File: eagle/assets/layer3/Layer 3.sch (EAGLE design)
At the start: 84 parts, among them Q2 AO3402, X1 SM06B-SRSS-TB, Y1 8MHz

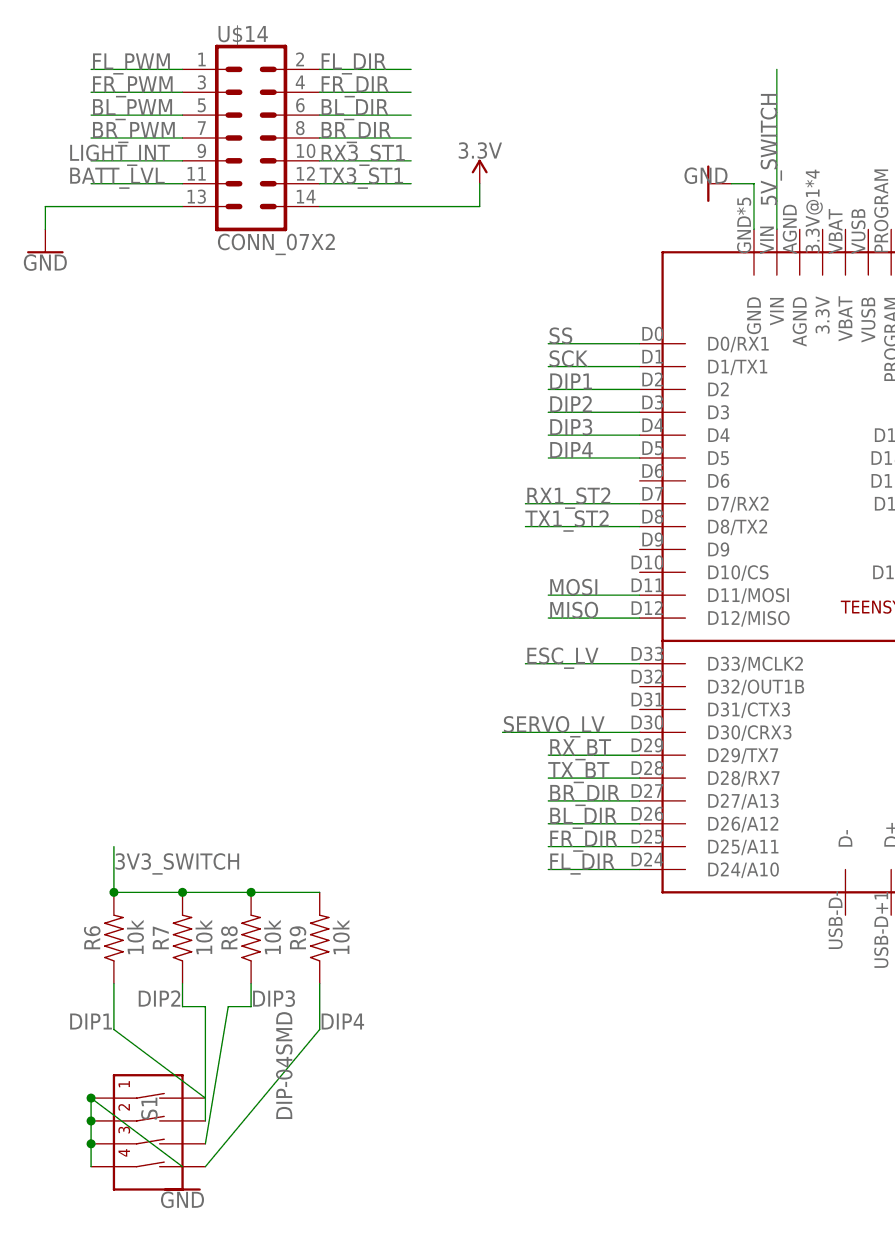
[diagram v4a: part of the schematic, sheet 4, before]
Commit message: added teensy 4 lbr
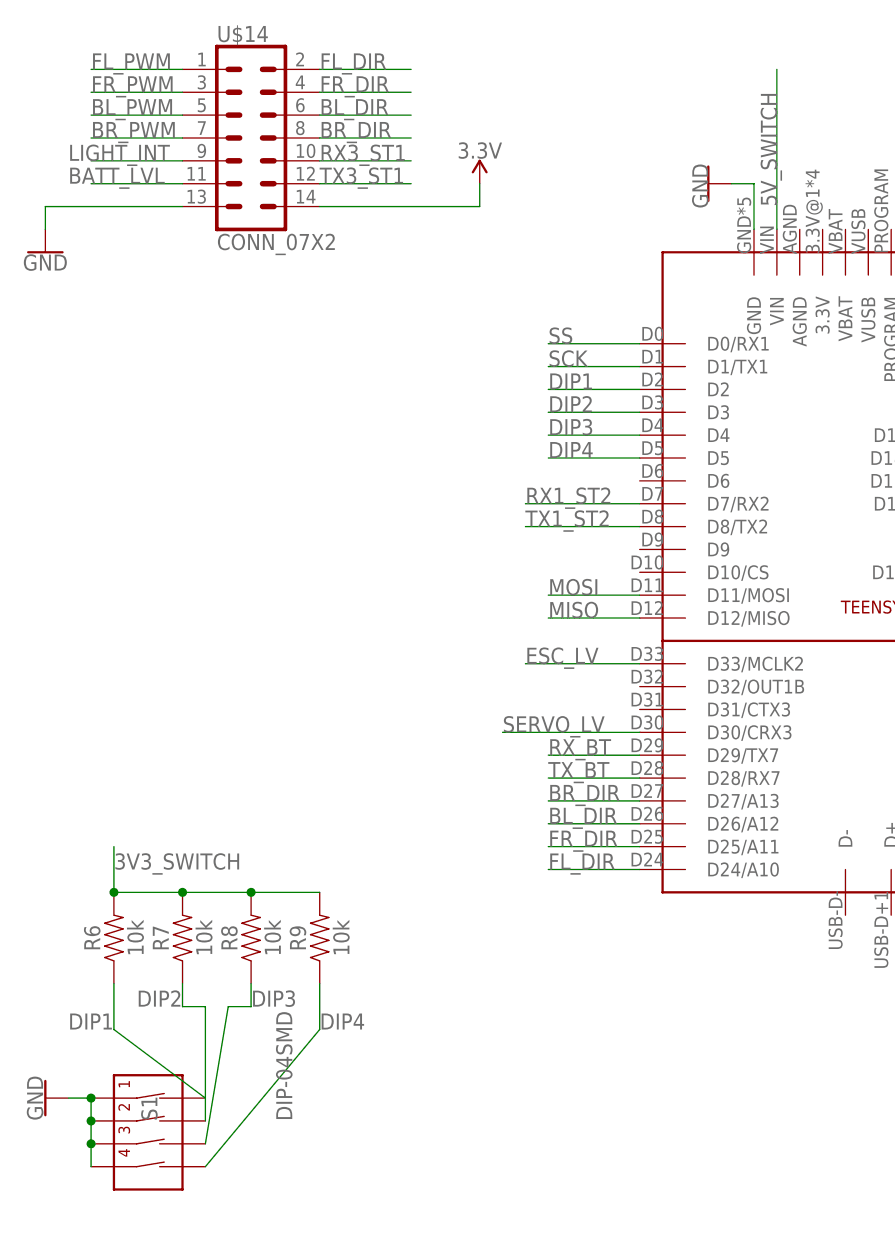
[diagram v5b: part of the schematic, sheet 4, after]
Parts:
- renumbered U$1 to TEENSY4
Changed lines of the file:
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@@
 <part name="R11" library="SparkFun-Resistors" library_urn="urn:adsk.eagle:library:532" deviceset="4.7KOHM" device="-0603-1/10W-1%" package3d_urn="urn:adsk.eagle:package:39650/1" value="4.7k"/>
 <part name="GND34" library="SparkFun-PowerSymbols" library_urn="urn:adsk.eagle:library:530" deviceset="GND" device=""/>
-<part name="U$1" library="Teensy-4.0" deviceset="TEENSY-4.0-FULL-BREAKOUT-PINS" device=""/>
+<part name="TEENSY4" library="Teensy-4.0" deviceset="TEENSY-4.0-FULL-BREAKOUT-PINS" device=""/>
 <part name="GND35" library="SparkFun-PowerSymbols" library_urn="urn:adsk.eagle:library:530" deviceset="GND" device=""/>
 </parts>
@@
 <attribute name="VALUE" x="43.434" y="38.1" size="1.778" layer="96" font="vector" rot="R90" align="top-left"/>
 </instance>
-<instance part="GND38" gate="1" x="33.02" y="30.48" smashed="yes">
-<attribute name="VALUE" x="33.02" y="30.226" size="1.778" layer="96" align="top-center"/>
+<instance part="GND38" gate="1" x="17.78" y="40.64" smashed="yes" rot="R270">
+<attribute name="VALUE" x="17.526" y="40.64" size="1.778" layer="96" rot="R270" align="top-center"/>
 </instance>
 <instance part="R6" gate="G$1" x="25.4" y="58.42" smashed="yes" rot="R90">
@@
 <attribute name="VALUE" x="246.38" y="106.934" size="1.778" layer="96" align="bottom-center"/>
 </instance>
-<instance part="U$1" gate="G$1" x="86.36" y="63.5" smashed="yes"/>
+<instance part="TEENSY4" gate="G$1" x="86.36" y="63.5" smashed="yes"/>
 <instance part="GND35" gate="1" x="91.44" y="142.24" smashed="yes" rot="R270">
-<attribute name="VALUE" x="91.186" y="142.24" size="1.778" layer="96" rot="R180" align="top-center"/>
+<attribute name="VALUE" x="91.44" y="141.986" size="1.778" layer="96" rot="R270" align="top-center"/>
 </instance>
 </instances>
@@
 </segment>
 <segment>
-<pinref part="U$1" gate="G$1" pin="D24/A10"/>
+<pinref part="TEENSY4" gate="G$1" pin="D24/A10"/>
 <wire x1="83.82" y1="66.04" x2="73.66" y2="66.04" width="0.1524" layer="91"/>
 <label x="73.66" y="66.04" size="1.778" layer="95"/>
@@
 </segment>
 <segment>
-<pinref part="U$1" gate="G$1" pin="D25/A11"/>
+<pinref part="TEENSY4" gate="G$1" pin="D25/A11"/>
 <wire x1="83.82" y1="68.58" x2="73.66" y2="68.58" width="0.1524" layer="91"/>
 <label x="73.66" y="68.58" size="1.778" layer="95"/>
@@
 </segment>
 <segment>
-<pinref part="U$1" gate="G$1" pin="D26/A12"/>
+<pinref part="TEENSY4" gate="G$1" pin="D26/A12"/>
 <wire x1="83.82" y1="71.12" x2="73.66" y2="71.12" width="0.1524" layer="91"/>
 <label x="73.66" y="71.12" size="1.778" layer="95"/>
@@
 </segment>
 <segment>
-<pinref part="U$1" gate="G$1" pin="D27/A13"/>
+<pinref part="TEENSY4" gate="G$1" pin="D27/A13"/>
 <wire x1="83.82" y1="73.66" x2="73.66" y2="73.66" width="0.1524" layer="91"/>
 <label x="73.66" y="73.66" size="1.778" layer="95"/>
@@
 <wire x1="129.54" y1="101.6" x2="147.32" y2="101.6" width="0.1524" layer="91"/>
 <label x="147.32" y="103.378" size="1.778" layer="95" rot="R180"/>
-<pinref part="U$1" gate="G$1" pin="D14/A0"/>
+<pinref part="TEENSY4" gate="G$1" pin="D14/A0"/>
 </segment>
 </net>
@@
 <wire x1="129.54" y1="99.06" x2="147.32" y2="99.06" width="0.1524" layer="91"/>
 <label x="147.32" y="100.838" size="1.778" layer="95" rot="R180"/>
-<pinref part="U$1" gate="G$1" pin="D13/SCK/LED"/>
+<pinref part="TEENSY4" gate="G$1" pin="D13/SCK/LED"/>
 </segment>
 </net>
@@
 </segment>
 <segment>
-<pinref part="U$1" gate="G$1" pin="D18/A4/SDA0"/>
+<pinref part="TEENSY4" gate="G$1" pin="D18/A4/SDA0"/>
 <wire x1="129.54" y1="111.76" x2="147.32" y2="111.76" width="0.1524" layer="91"/>
 <label x="134.62" y="111.76" size="1.778" layer="95"/>
@@
 </segment>
 <segment>
-<pinref part="U$1" gate="G$1" pin="D19/A5/SCL0"/>
+<pinref part="TEENSY4" gate="G$1" pin="D19/A5/SCL0"/>
 <wire x1="129.54" y1="114.3" x2="147.32" y2="114.3" width="0.1524" layer="91"/>
 <label x="134.62" y="114.3" size="1.778" layer="95"/>
@@
 </segment>
 <segment>
-<pinref part="U$1" gate="G$1" pin="D20/A6"/>
+<pinref part="TEENSY4" gate="G$1" pin="D20/A6"/>
 <wire x1="129.54" y1="116.84" x2="147.32" y2="116.84" width="0.1524" layer="91"/>
 <label x="134.62" y="116.84" size="1.778" layer="95"/>
@@
 </segment>
 <segment>
-<pinref part="U$1" gate="G$1" pin="D21/A7"/>
+<pinref part="TEENSY4" gate="G$1" pin="D21/A7"/>
 <wire x1="129.54" y1="119.38" x2="147.32" y2="119.38" width="0.1524" layer="91"/>
 <label x="134.62" y="119.38" size="1.778" layer="95"/>
@@
 <wire x1="129.54" y1="121.92" x2="147.32" y2="121.92" width="0.1524" layer="91"/>
 <label x="134.62" y="121.92" size="1.778" layer="95"/>
-<pinref part="U$1" gate="G$1" pin="D22/A8"/>
+<pinref part="TEENSY4" gate="G$1" pin="D22/A8"/>
 </segment>
 </net>
@@
 <wire x1="129.54" y1="124.46" x2="147.32" y2="124.46" width="0.1524" layer="91"/>
 <label x="134.62" y="124.46" size="1.778" layer="95"/>
-<pinref part="U$1" gate="G$1" pin="D23/A9"/>
+<pinref part="TEENSY4" gate="G$1" pin="D23/A9"/>
 </segment>
 </net>
@@
 <junction x="22.86" y="35.56"/>
 <pinref part="GND38" gate="1" pin="GND"/>
-<wire x1="22.86" y1="40.64" x2="33.02" y2="33.02" width="0.1524" layer="91"/>
+<wire x1="22.86" y1="40.64" x2="20.32" y2="40.64" width="0.1524" layer="91"/>
 <junction x="22.86" y="40.64"/>
 </segment>
@@
 </segment>
 <segment>
-<pinref part="U$1" gate="G$1" pin="GND"/>
+<pinref part="TEENSY4" gate="G$1" pin="GND"/>
 <wire x1="96.52" y1="137.16" x2="96.52" y2="142.24" width="0.1524" layer="91"/>
 <wire x1="96.52" y1="142.24" x2="93.98" y2="142.24" width="0.1524" layer="91"/>
@@
 </segment>
 <segment>
-<pinref part="U$1" gate="G$1" pin="VIN"/>
+<pinref part="TEENSY4" gate="G$1" pin="VIN"/>
 <wire x1="99.06" y1="137.16" x2="99.06" y2="154.94" width="0.1524" layer="91"/>
 <label x="99.06" y="139.7" size="1.778" layer="95" rot="R90"/>
@@
 </segment>
 <segment>
-<pinref part="U$1" gate="G$1" pin="D11/MOSI"/>
+<pinref part="TEENSY4" gate="G$1" pin="D11/MOSI"/>
 <wire x1="83.82" y1="96.52" x2="73.66" y2="96.52" width="0.1524" layer="91"/>
 <label x="73.66" y="96.52" size="1.778" layer="95"/>
@@
 </segment>
 <segment>
-<pinref part="U$1" gate="G$1" pin="D12/MISO"/>
+<pinref part="TEENSY4" gate="G$1" pin="D12/MISO"/>
 <wire x1="83.82" y1="93.98" x2="73.66" y2="93.98" width="0.1524" layer="91"/>
 <label x="73.66" y="93.98" size="1.778" layer="95"/>
@@
 </segment>
 <segment>
-<pinref part="U$1" gate="G$1" pin="D1/TX1"/>
+<pinref part="TEENSY4" gate="G$1" pin="D1/TX1"/>
 <wire x1="83.82" y1="121.92" x2="73.66" y2="121.92" width="0.1524" layer="91"/>
 <label x="73.66" y="121.92" size="1.778" layer="95"/>
@@
 </segment>
 <segment>
-<pinref part="U$1" gate="G$1" pin="D0/RX1"/>
+<pinref part="TEENSY4" gate="G$1" pin="D0/RX1"/>
 <wire x1="83.82" y1="124.46" x2="73.66" y2="124.46" width="0.1524" layer="91"/>
 <label x="73.66" y="124.46" size="1.778" layer="95"/>
@@
 <wire x1="129.54" y1="106.68" x2="147.32" y2="106.68" width="0.1524" layer="91"/>
 <label x="134.62" y="106.68" size="1.778" layer="95"/>
-<pinref part="U$1" gate="G$1" pin="D16/A2/SCL1"/>
+<pinref part="TEENSY4" gate="G$1" pin="D16/A2/SCL1"/>
 </segment>
 </net>
@@
 <wire x1="129.54" y1="109.22" x2="147.32" y2="109.22" width="0.1524" layer="91"/>
 <label x="134.62" y="109.22" size="1.778" layer="95"/>
-<pinref part="U$1" gate="G$1" pin="D17/A3/SDA1"/>
+<pinref part="TEENSY4" gate="G$1" pin="D17/A3/SDA1"/>
 </segment>
 </net>
@@
 <wire x1="83.82" y1="119.38" x2="73.66" y2="119.38" width="0.1524" layer="91"/>
 <label x="73.66" y="119.38" size="1.778" layer="95"/>
-<pinref part="U$1" gate="G$1" pin="D2"/>
+<pinref part="TEENSY4" gate="G$1" pin="D2"/>
 </segment>
 </net>
@@
 <wire x1="83.82" y1="116.84" x2="73.66" y2="116.84" width="0.1524" layer="91"/>
 <label x="73.66" y="116.84" size="1.778" layer="95"/>
-<pinref part="U$1" gate="G$1" pin="D3"/>
+<pinref part="TEENSY4" gate="G$1" pin="D3"/>
 </segment>
 </net>
@@
 <wire x1="83.82" y1="114.3" x2="73.66" y2="114.3" width="0.1524" layer="91"/>
 <label x="73.66" y="114.3" size="1.778" layer="95"/>
-<pinref part="U$1" gate="G$1" pin="D4"/>
+<pinref part="TEENSY4" gate="G$1" pin="D4"/>
 </segment>
 </net>
@@
 <wire x1="83.82" y1="111.76" x2="73.66" y2="111.76" width="0.1524" layer="91"/>
 <label x="73.66" y="111.76" size="1.778" layer="95"/>
-<pinref part="U$1" gate="G$1" pin="D5"/>
+<pinref part="TEENSY4" gate="G$1" pin="D5"/>
 </segment>
 </net>
@@
 <wire x1="83.82" y1="78.74" x2="73.66" y2="78.74" width="0.1524" layer="91"/>
 <label x="73.66" y="78.74" size="1.778" layer="95"/>
-<pinref part="U$1" gate="G$1" pin="D29/TX7"/>
+<pinref part="TEENSY4" gate="G$1" pin="D29/TX7"/>
 </segment>
 </net>
@@
 <wire x1="83.82" y1="76.2" x2="73.66" y2="76.2" width="0.1524" layer="91"/>
 <label x="73.66" y="76.2" size="1.778" layer="95"/>
-<pinref part="U$1" gate="G$1" pin="D28/RX7"/>
+<pinref part="TEENSY4" gate="G$1" pin="D28/RX7"/>
 </segment>
 </net>
@@
 <wire x1="83.82" y1="88.9" x2="71.12" y2="88.9" width="0.1524" layer="91"/>
 <label x="71.12" y="88.9" size="1.778" layer="95"/>
-<pinref part="U$1" gate="G$1" pin="D33/MCLK2"/>
+<pinref part="TEENSY4" gate="G$1" pin="D33/MCLK2"/>
 </segment>
 </net>
@@
 <wire x1="83.82" y1="81.28" x2="68.58" y2="81.28" width="0.1524" layer="91"/>
 <label x="68.58" y="81.28" size="1.778" layer="95"/>
-<pinref part="U$1" gate="G$1" pin="D30/CRX3"/>
+<pinref part="TEENSY4" gate="G$1" pin="D30/CRX3"/>
 </segment>
 </net>
@@
 <wire x1="83.82" y1="106.68" x2="71.12" y2="106.68" width="0.1524" layer="91"/>
 <label x="71.12" y="106.68" size="1.778" layer="95"/>
-<pinref part="U$1" gate="G$1" pin="D7/RX2"/>
+<pinref part="TEENSY4" gate="G$1" pin="D7/RX2"/>
 </segment>
 </net>
@@
 <wire x1="83.82" y1="104.14" x2="71.12" y2="104.14" width="0.1524" layer="91"/>
 <label x="71.12" y="104.14" size="1.778" layer="95"/>
-<pinref part="U$1" gate="G$1" pin="D8/TX2"/>
-</segment>
-</net>
+<pinref part="TEENSY4" gate="G$1" pin="D8/TX2"/>
+</segment>
+</net>
